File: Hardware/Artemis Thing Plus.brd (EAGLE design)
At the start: 22.9 x 58.4 mm, 130 parts, among them J2 CORTEX_DEBUG, J5 USB-C, U1 MCP73831, U2 3.3V, U3 ARTEMIS_MODULESMD, U4 CH340E_MSOP10, Y1 32.768kHz

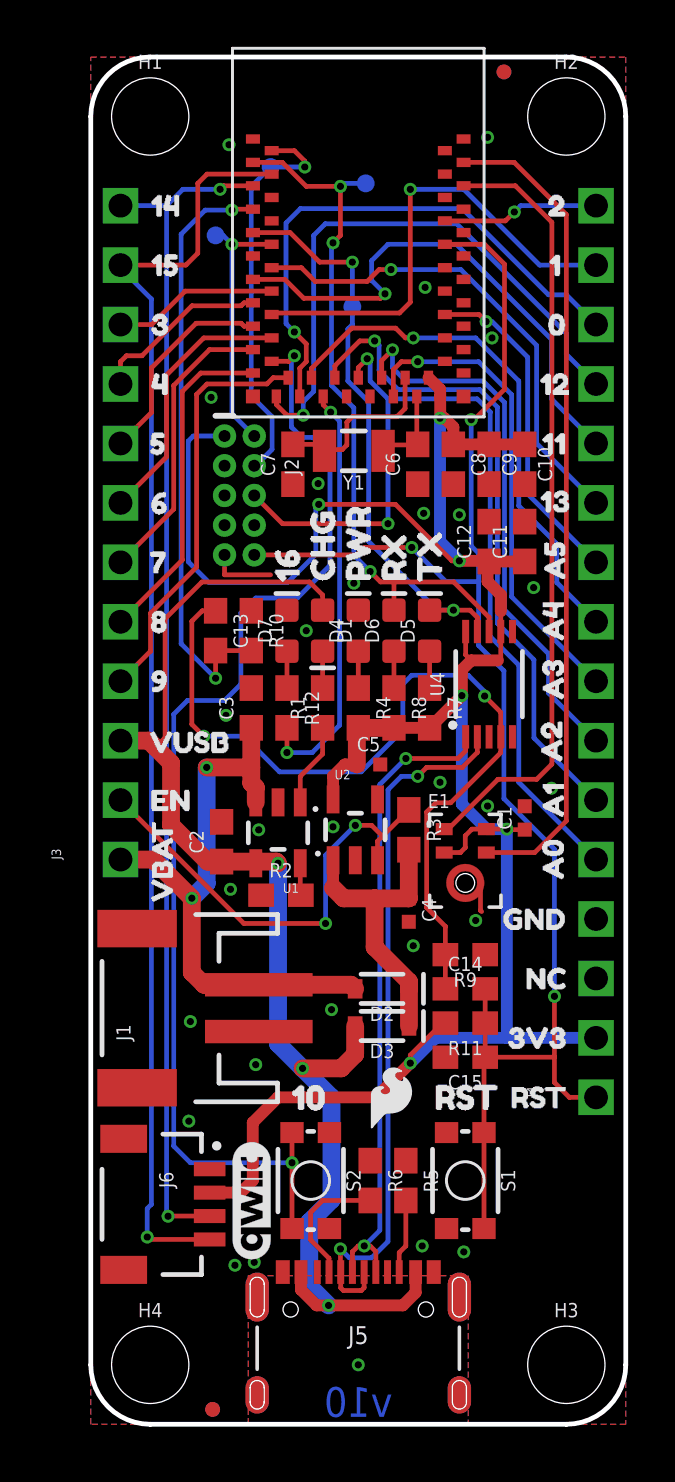
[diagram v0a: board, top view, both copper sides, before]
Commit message: v10 Update
Schematic:
- Change 100k pull-down resistor in bootloader circuit to DNP
- Replaced diodes with lower forward voltage drop
- Added second I2C Bus to breakout pins. All broken out pins are now PWM capable
- Replaced 4.7k LEDs resistors to 1k for all LEDs
- Added testpoints for Qwiic data lines

Layout:
- Removed "~" for PWM pins as all pins now support PWM
- Increased flame logo
- Fixed USB traces
- Labeled microphone
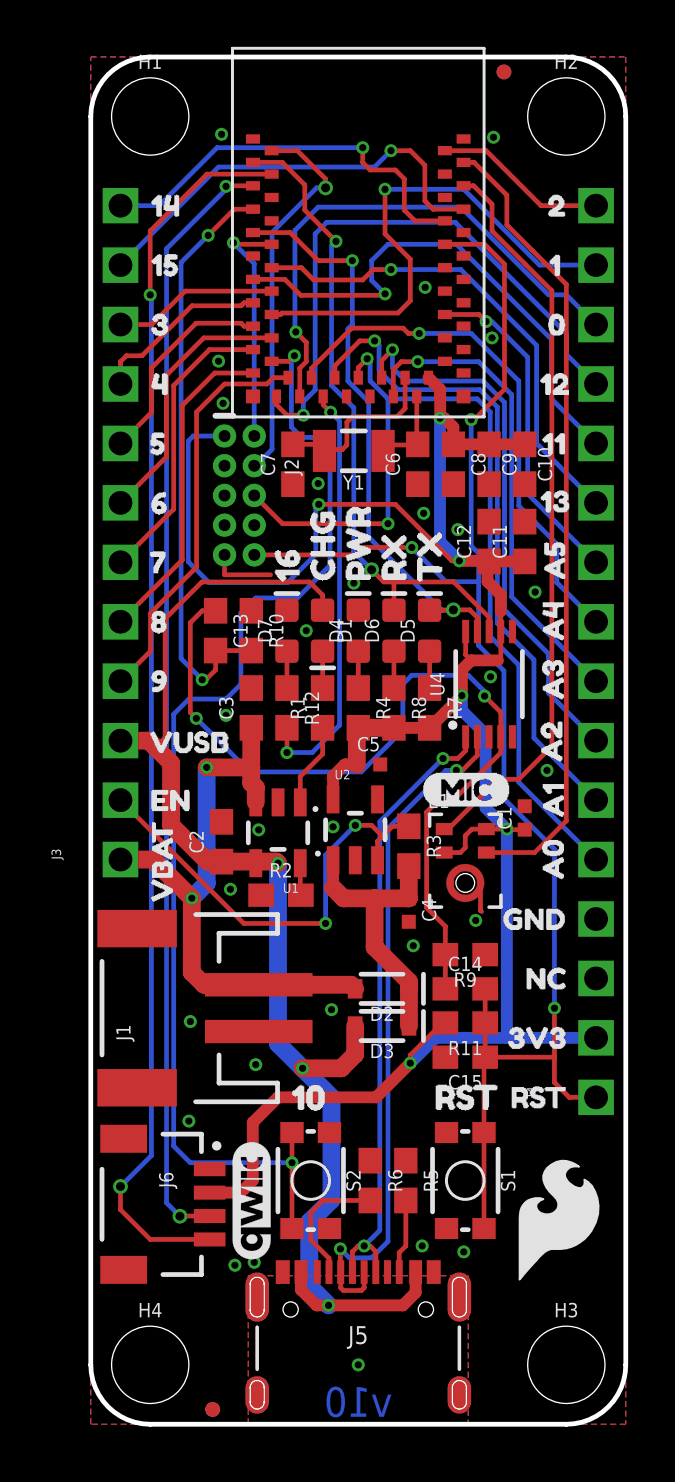
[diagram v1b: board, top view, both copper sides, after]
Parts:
- added TP5: TEST-POINTTP_15TH_THRU, SparkFun-Connectors:TP_15TH
- added U$66: (no value), buzzard_labels (10):MIC0
- D2, D3: value 1A/23V/620mV -> 3A/10V/280mV
- R7, R8: value 4.7k -> 1k
- R9: value 100k -> DNP
- TP1: device SparkFun-Connectors:PAD.03X.03 -> SparkFun-Connectors:TP_15TH
- TP2, TP3, TP4: value (none) -> TEST-POINTTP_15TH_THRU; device SparkFun-Connectors:PAD.03X.03 -> SparkFun-Connectors:TP_15TH
- U$34: device buzzard_labels (2):2#0 -> buzzard_labels (6):20
- U$35: device buzzard_labels (2):1##TX12 -> buzzard_labels (6):1#TX11
- U$36: device buzzard_labels (2):0##RX13 -> buzzard_labels (6):0#RX12
- U$37: device buzzard_labels (2):12##MISO1 -> buzzard_labels (6):12#MISO3
- U$38: device buzzard_labels (2):11##MOSI4 -> buzzard_labels (6):11#MOSI4
- U$39: device buzzard_labels (2):13##SCK5 -> buzzard_labels (6):13#SCK5
- U$40: device buzzard_labels (4):A5#0 -> buzzard_labels (6):A56
- U$41: device buzzard_labels (4):A4#1 -> buzzard_labels (6):A47
- U$42: device buzzard_labels (4):A3#2 -> buzzard_labels (6):A38
- U$43: device buzzard_labels (4):A2#3 -> buzzard_labels (6):A29
- U$44: device buzzard_labels (4):A1#4 -> buzzard_labels (6):A110
- U$45: device buzzard_labels (4):A0#5 -> buzzard_labels (6):A011
- U$50: device buzzard_labels (2):SDA#1416 -> buzzard_labels (8):14#SDA10
- U$51: device buzzard_labels (2):SCL#15#17 -> buzzard_labels (8):15#SCL11
- U$52: device buzzard_labels (2):3##A618 -> buzzard_labels (6):412
- U$53: device buzzard_labels (2):4#19 -> buzzard_labels (6):513
- U$54: device buzzard_labels (2):5#20 -> buzzard_labels (6):614
- U$55: device buzzard_labels (2):6#21 -> buzzard_labels (6):715
- U$56: device buzzard_labels (2):7#22 -> buzzard_labels (6):816
- U$57: device buzzard_labels (2):8#23 -> buzzard_labels (6):9#A719
- U$58: device buzzard_labels (2):9##A724 -> buzzard_labels (7):3#A60
- U$65: device SparkFun-Aesthetics:SFE_LOGO_FLAME_.1 -> SparkFun-Aesthetics:SFE_LOGO_FLAME_.2
- moved TP4 38.9 mm to (1.27, 10.2), flipped to the top
- moved LOGO1 22.5 mm to (10.8, 19.1)
- moved TP3 18.6 mm to (15.5, 34.8), flipped to the top
- moved TP2 15.8 mm to (12.0, 36.5), flipped to the top
- moved U$58 15.3 mm to (6.88, 47.0)
- moved U$65 8.90 mm to (20.0, 8.70)
- moved U$52 4.47 mm to (4.20, 44.5)
- moved U$57 3.00 mm to (6.79, 31.8)
- moved U$53 2.76 mm to (4.11, 41.9)
- moved U$56 2.73 mm to (4.15, 34.3)
- moved U$55 2.73 mm to (4.16, 36.8)
- moved U$54 2.72 mm to (4.16, 39.4)
- moved TP1 2.51 mm to (10.0, 52.8), flipped to the top
- moved R3 0.70 mm to (13.6, 24.7)
- moved U$50 0.55 mm to (9.00, 52.1)
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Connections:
- net ~D17/A0 renamed ~D18/A0
- net ~D18/A1 renamed ~D19/A1
- net ~D19/A2 renamed ~D20/A2
- net ~D20/A3 renamed ~D21/A3
- net ~D21/A4 renamed ~D22/A4
- net ~D22/A5 renamed ~D23/A5
- removed net D14/SDA: J3.12, J6.3, U3.D40
- removed net ~D15/SCL: J3.11, J6.4, U3.~D39
- new net D14/QWIIC_SDA: J6.3, TP5.P$1, U3.D40
- new net ~D15/QWIIC_SCL: J6.4, TP4.P$1, U3.~D39
- new net ~D16/SDA1: J3.12, U3.~D43
- new net ~D17/SCL1: J3.11, U3.~D42
- net RXI-0: now also TP2.P$1; no longer TP3.P$1
- net SWDIO: no longer TP2.P$1
- net TXO-0: now also TP3.P$1; no longer TP4.P$1
- net ~D2: now also U3.~D44; no longer U3.~D43
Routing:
- net ~D15/SCL: track 54.7 -> 0.00 mm, vias 1 -> 0
- net ~D15/QWIIC_SCL: track 0.00 -> 52.9 mm, vias 0 -> 1
- net D14/SDA: track 51.0 -> 0.00 mm, vias 2 -> 0
- net D14/QWIIC_SDA: track 0.00 -> 47.7 mm, vias 0 -> 1
- net ~D17/SCL1: track 0.00 -> 18.6 mm, vias 0 -> 1
- net ~D16/SDA1: track 0.00 -> 17.3 mm, vias 0 -> 1
- net RXI-0: track 30.3 -> 28.1 mm, vias 3 -> 1
- net PDMDATA: track 33.3 -> 31.8 mm
- net ~D1/TXO-1: track 20.2 -> 21.7 mm
- net PDMCLK: track 35.2 -> 34.2 mm
- net D+1: track 27.8 -> 26.9 mm
- net D-1: track 30.4 -> 29.5 mm
- net SWDIO: track 11.1 -> 10.3 mm
- net ~D2: track 6.73 -> 7.43 mm, vias 1 -> 0
- net VIN: track 12.7 -> 12.0 mm
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
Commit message: v10 design review changes
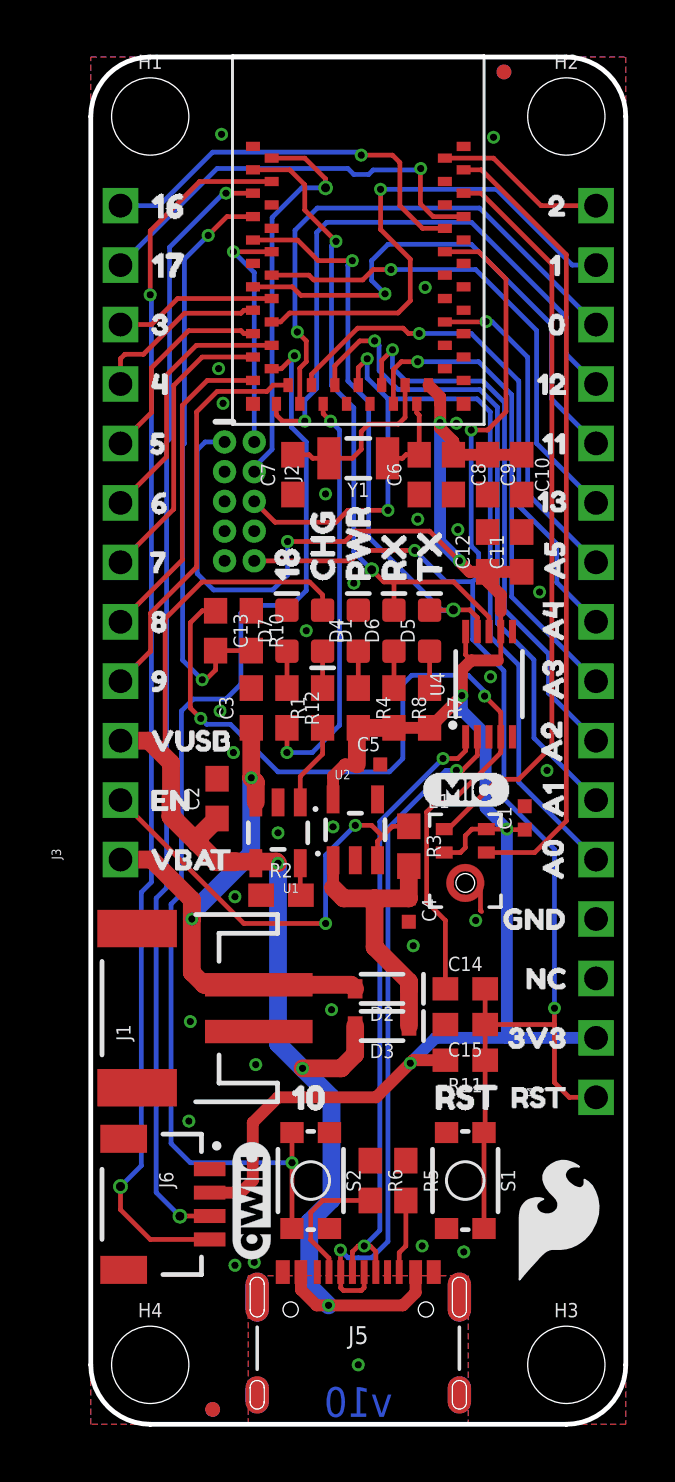
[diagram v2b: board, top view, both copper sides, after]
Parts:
- removed R9: DNP, SparkFun-Resistors:0603
- C13: value 2.2uF -> 0.1uF
- R10: value 10k -> 220k
- U$1: device buzzard_labels:140 -> buzzard_labels (11):160
- U$2: device buzzard_labels:151 -> buzzard_labels (11):171
- U$29: device buzzard_labels (1):160 -> buzzard_labels (11):184
- U$50: device buzzard_labels (8):14#SDA10 -> buzzard_labels (11):16#SDA12
- U$51: device buzzard_labels (8):15#SCL11 -> buzzard_labels (11):17#SCL13
- moved U$64 18.5 mm to (13.5, 38.4), turned to 270 degrees
- moved U$12 2.90 mm to (1.78, 24.1), turned to 0 degrees
- moved C2 1.85 mm to (5.40, 26.7)
- moved LOGO1 1.80 mm to (12.1, 17.8), turned to 270 degrees
- moved LOGO3 1.75 mm to (10.9, 28.7), turned to 270 degrees
- moved R11 1.59 mm to (16.0, 15.6)
- moved C15 1.40 mm to (16.0, 17.1)
- moved C10 0.46 mm to (18.4, 40.6)
- moved C11 0.46 mm to (18.4, 37.3)
- moved C12 0.45 mm to (17.0, 37.3)
- moved C9 0.45 mm to (17.0, 40.6)
- moved C6 0.45 mm to (14.0, 40.6)
- moved C7 0.44 mm to (8.64, 40.6)
- moved C8 0.44 mm to (15.5, 40.6)
- moved Y1 0.37 mm to (11.4, 41.3)
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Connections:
- net ~D16/LED renamed ~D18/LED
- net ~D18/A0 renamed ~D19/A0
- net ~D19/A1 renamed ~D20/A1
- net ~D20/A2 renamed ~D21/A2
- net ~D21/A3 renamed ~D22/A3
- net ~D22/A4 renamed ~D23/A4
- net ~D23/A5 renamed ~D24/A5
- net !RTS: no longer R9.2
- net GND: no longer R9.1
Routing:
- net 3.3V: track 98.3 -> 94.9 mm
- net GND: track 7.18 -> 4.36 mm, vias 28 -> 29
- net V_USB: track 55.8 -> 57.0 mm
- net D10/SWCH: track 50.0 -> 49.1 mm
- net ~D12/MISO: track 25.2 -> 26.0 mm
- net V_BATT: track 25.2 -> 24.5 mm
- net !RTS: track 36.9 -> 37.5 mm

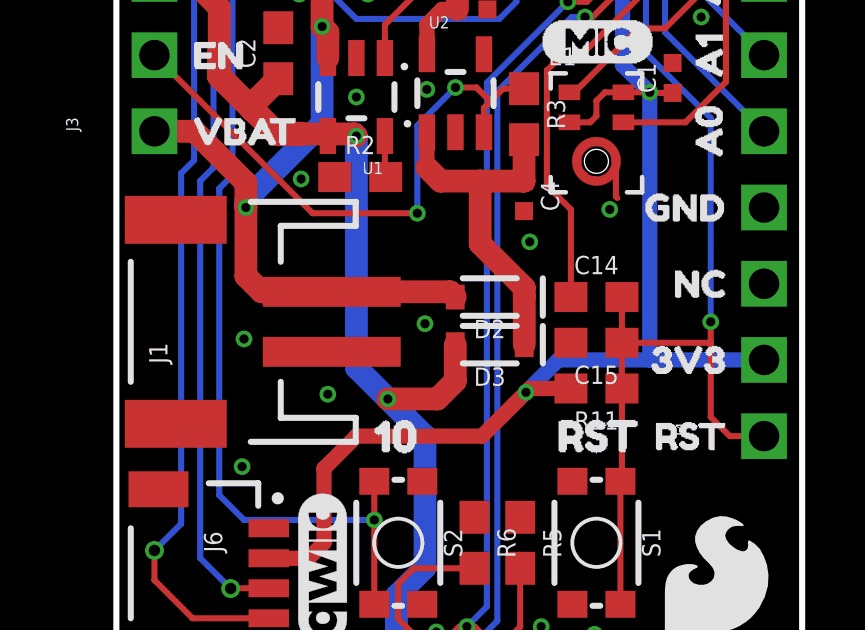
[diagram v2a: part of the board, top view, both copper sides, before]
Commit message: v10 QC fixes
Added + and - symbols to JST connector
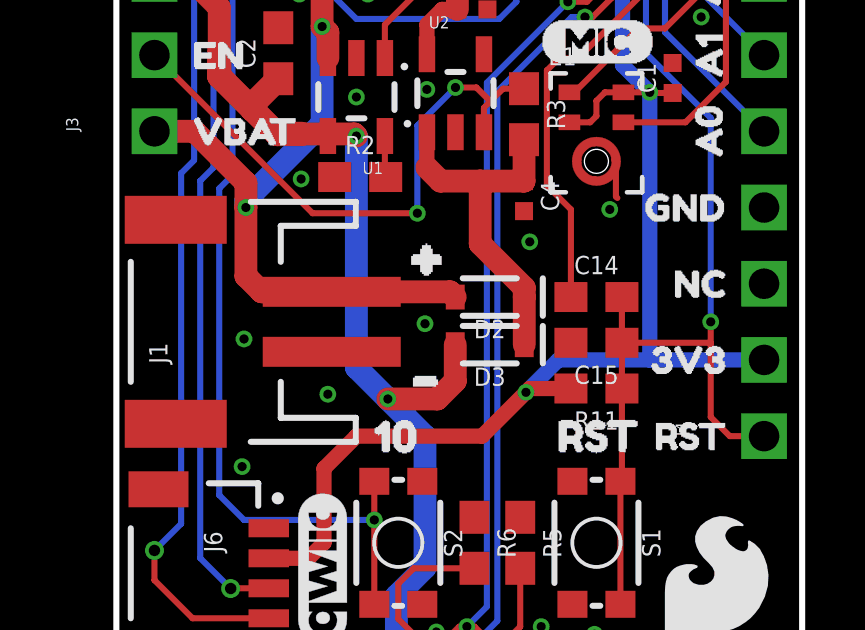
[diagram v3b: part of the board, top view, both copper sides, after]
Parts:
- added U$67: (no value), buzzard_labels (13):#0
- added U$68: (no value), buzzard_labels (13):#1
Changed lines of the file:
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@@
 <layer number="27" name="tValues" color="7" fill="1" visible="no" active="yes"/>
 <layer number="28" name="bValues" color="7" fill="1" visible="no" active="yes"/>
-<layer number="29" name="tStop" color="7" fill="3" visible="no" active="yes"/>
+<layer number="29" name="tStop" color="7" fill="3" visible="yes" active="yes"/>
 <layer number="30" name="bStop" color="7" fill="6" visible="no" active="yes"/>
 <layer number="31" name="tCream" color="7" fill="4" visible="no" active="yes"/>
@@
 <layer number="49" name="Reference" color="7" fill="1" visible="yes" active="yes"/>
 <layer number="50" name="dxf" color="7" fill="1" visible="no" active="no"/>
-<layer number="51" name="tDocu" color="7" fill="1" visible="yes" active="yes"/>
-<layer number="52" name="bDocu" color="7" fill="1" visible="yes" active="yes"/>
+<layer number="51" name="tDocu" color="61" fill="1" visible="yes" active="yes"/>
+<layer number="52" name="bDocu" color="6" fill="1" visible="yes" active="yes"/>
 <layer number="53" name="tGND_GNDA" color="7" fill="9" visible="no" active="no"/>
 <layer number="54" name="bGND_GNDA" color="1" fill="9" visible="no" active="no"/>
@@
 <element name="FD4" library="SparkFun-Aesthetics" package="FIDUCIAL-MICRO" value="FIDUCIALUFIDUCIAL" x="5.207" y="0.635" smashed="yes"/>
 <element name="FRAME1" library="SparkFun-Aesthetics" package="CREATIVE_COMMONS" value="FRAME-LETTER" x="-12.7" y="-20.32" smashed="yes">
-<attribute name="DESIGNER" value="" x="67.31" y="-31.75" size="1.778" layer="27" display="off"/>
-<attribute name="REV" value="" x="67.31" y="-31.75" size="1.778" layer="27" display="off"/>
+<attribute name="DESIGNER" value="Alex Wende" x="67.31" y="-31.75" size="1.778" layer="27" display="off"/>
+<attribute name="REV" value="v10" x="67.31" y="-31.75" size="1.778" layer="27" display="off"/>
 </element>
 <element name="FRAME2" library="SparkFun-Aesthetics" package="DUMMY" value="FRAME-LETTERNO_PACKAGE" x="-12.7" y="-20.32" smashed="yes">
@@
 <element name="U$2" library="buzzard_labels (11)" package="171" value="" x="1.7145" y="49.53" smashed="yes"/>
 <element name="U$29" library="buzzard_labels (11)" package="184" value="" x="8.382" y="35.1155" smashed="yes" rot="R90"/>
+<element name="U$67" library="buzzard_labels (13)" package="#0" value="" x="8.4455" y="20.066" smashed="yes"/>
+<element name="U$68" library="buzzard_labels (13)" package="#1" value="" x="8.4455" y="16.129" smashed="yes"/>
 </elements>
 <signals>
